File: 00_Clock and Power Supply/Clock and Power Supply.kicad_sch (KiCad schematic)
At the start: 2 parts, among them J1 Output 1, J2 Output 2

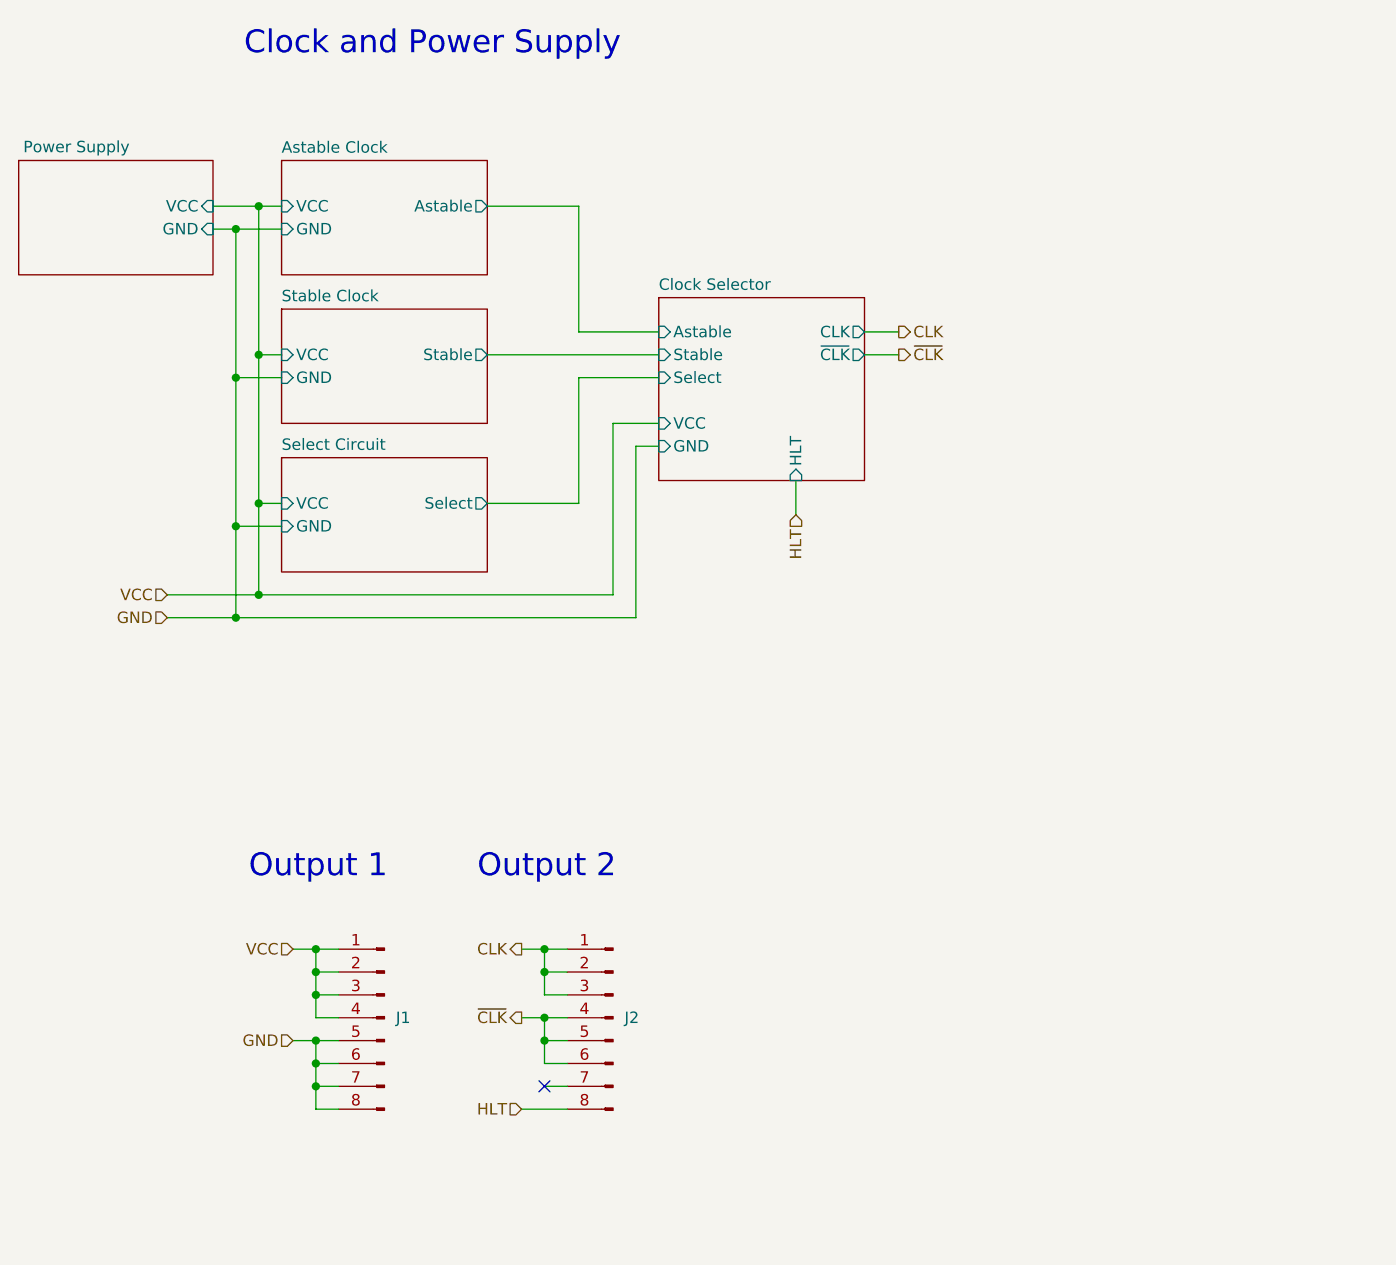
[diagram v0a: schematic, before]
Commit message: Last revision of the cpu, all boards have been ordered. Implementation to be tested and documented in following commits.
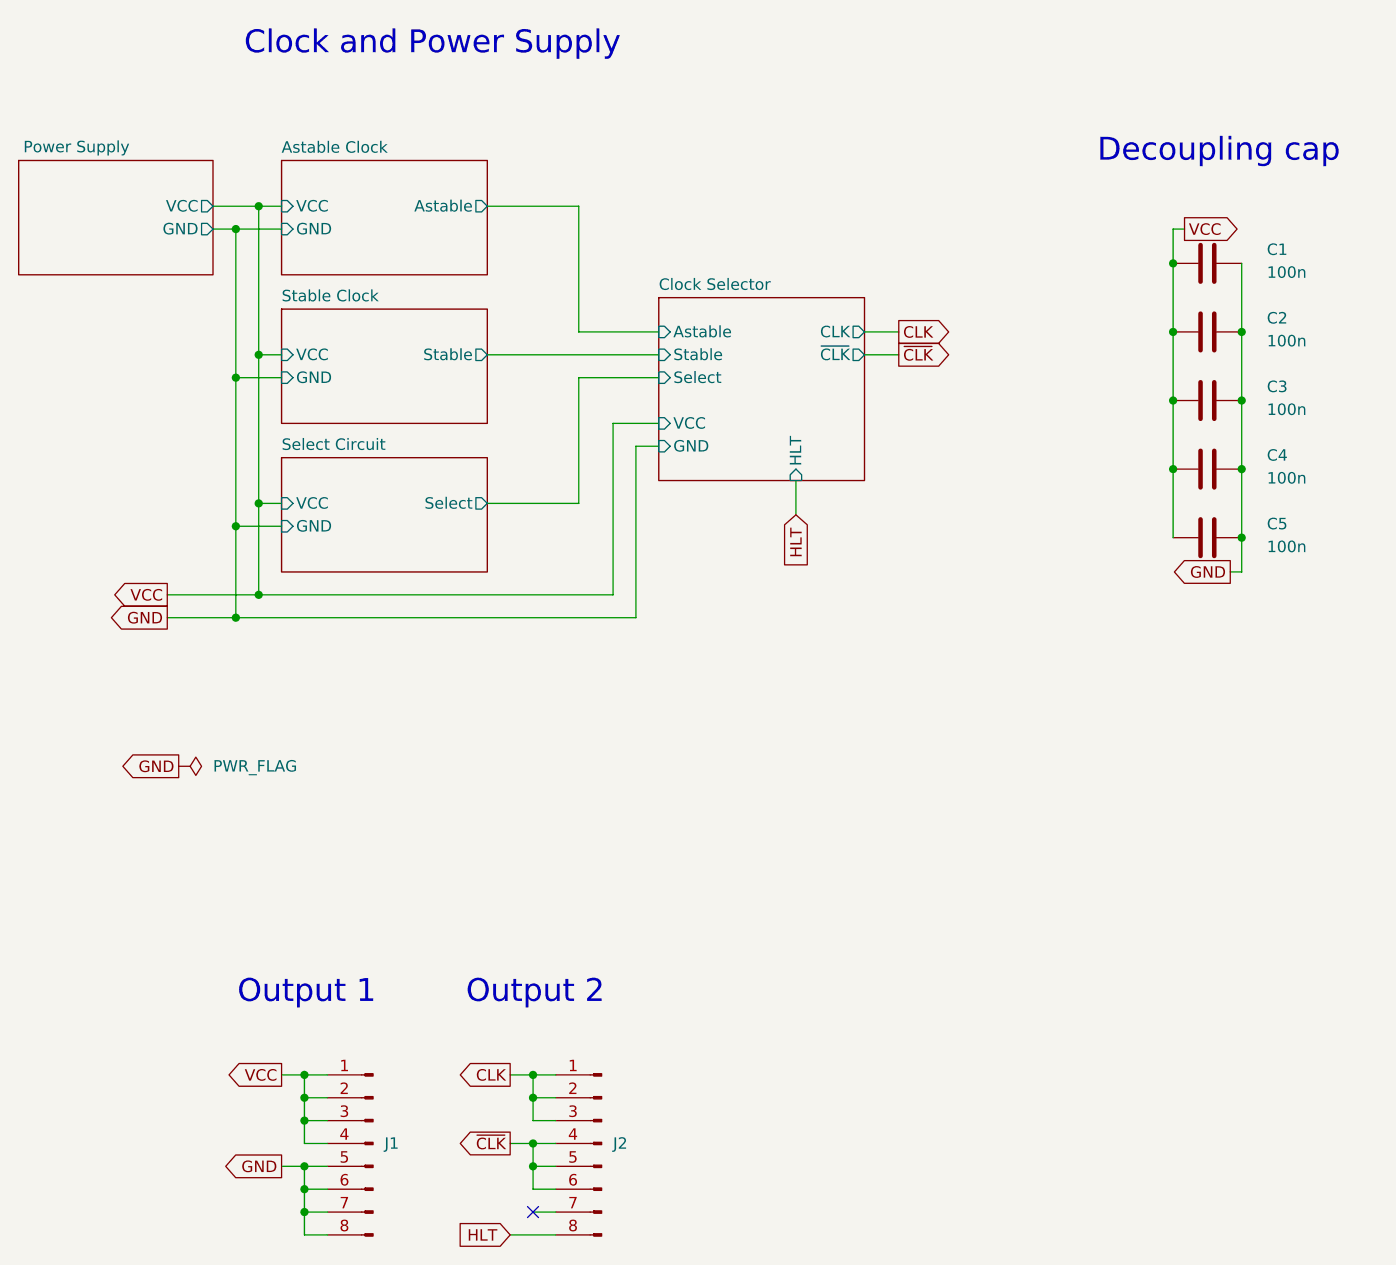
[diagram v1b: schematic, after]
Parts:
- added C1, C2, C3, C4, C5: 100n, Capacitor_THT:C_Disc_D3.0mm_W1.6mm_P2.50mm, symbol Device:C
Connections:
- net GND: now also C1.2, C2.2, C3.2, C4.2, C5.2
- net VCC: now also C1.1, C2.1, C3.1, C4.1, C5.1
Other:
- note added: "Decoupling cap"
- moved on the sheet: J1, J2
